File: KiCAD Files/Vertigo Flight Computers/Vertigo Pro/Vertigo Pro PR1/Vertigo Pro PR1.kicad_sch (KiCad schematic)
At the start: 140 parts, among them IC1 ICM-20602, IC2 DPS310XTSA1, IC3 MLX90393SLW-ABA-011-RE, J1 ST-LINK Conn, J2 USB_C_Receptacle_USB2.0, J3 FFC2A32-24-T, J4 Screw_Terminal, J5 Screw_Terminal, J6 Screw_Terminal, J7 Screw_Terminal, Q1 IRF530SPBF, Q2 IRF530SPBF, Q3 IRF530SPBF, Q4 IRF530SPBF, SW1 SW_SPDT, U1 STM32F103C8Tx, U10 TPS79133DBVR, U11 TLV709, U12 TLV709, U2 AP63203WU, U3 ESP32-S3-WROOM-1, U4 ME6211C28M5G-N, U5 ME6211C15M5G-N, U6 W25Q64FV, U7 TPS2121RUXR, U8 NEO-6M-GPS, U9 24AA32A-I_MS, Y1 16MHz

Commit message: sth
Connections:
- net STM_UART_RX is gone; now on net ESP_UART_TX: U1.31 (PA10), U8.20 (TXD1)
- net STM_UART_TX is gone; now on net ESP_UART_RX: U1.30 (PA9), U8.21 (RXD1)
- net ESP_UART_RX: now reaches U3.36 (RXD0)
- net ESP_UART_TX: now reaches U3.37 (TXD0)
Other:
- note added: "UART Communication MuCU/TuCU"
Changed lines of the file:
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@@
 	(wire
 		(pts
+			(xy 128.27 170.18) (xy 142.24 170.18)
+		)
+		(stroke
+			(width 0)
+			(type default)
+		)
+	)
+	(wire
+		(pts
 			(xy 58.42 262.89) (xy 69.85 262.89)
 		)
@@
 	(wire
 		(pts
+			(xy 158.75 144.78) (xy 187.96 144.78)
+		)
+		(stroke
+			(width 0)
+			(type default)
+		)
+	)
+	(wire
+		(pts
 			(xy 511.81 194.31) (xy 518.16 194.31)
 		)
@@
 	(wire
 		(pts
-			(xy 128.27 172.72) (xy 140.97 172.72)
+			(xy 128.27 172.72) (xy 142.24 172.72)
 		)
 		(stroke
@@
 	(wire
 		(pts
+			(xy 158.75 148.59) (xy 187.96 148.59)
+		)
+		(stroke
+			(width 0)
+			(type default)
+		)
+	)
+	(wire
+		(pts
 			(xy 486.41 288.29) (xy 501.65 288.29)
 		)
@@
 	(wire
 		(pts
-			(xy 128.27 175.26) (xy 140.97 175.26)
+			(xy 128.27 175.26) (xy 142.24 175.26)
 		)
 		(stroke
@@
 	(wire
 		(pts
+			(xy 128.27 167.64) (xy 142.24 167.64)
+		)
+		(stroke
+			(width 0)
+			(type default)
+		)
+	)
+	(wire
+		(pts
 			(xy 557.53 87.63) (xy 565.15 87.63)
 		)
@@
 		)
 	)
+	(text "UART Communication MuCU/TuCU"
+		(exclude_from_sim no)
+		(at 173.99 139.7 0)
+		(effects
+			(font
+				(size 1.27 1.27)
+			)
+		)
+	)
 	(text "Channel 4\n"
 		(exclude_from_sim no)
@@
 		)
 	)
+	(label "STM_UART_RX"
+		(at 187.96 148.59 180)
+		(fields_autoplaced yes)
+		(effects
+			(font
+				(size 1.27 1.27)
+			)
+			(justify right bottom)
+		)
+	)
 	(label "ESP_I2C_SCL"
 		(at 85.09 185.42 0)
@@
 		)
 	)
+	(label "ESP_UART_TX"
+		(at 158.75 148.59 0)
+		(fields_autoplaced yes)
+		(effects
+			(font
+				(size 1.27 1.27)
+			)
+			(justify left bottom)
+		)
+	)
 	(label "CAM_RESET"
 		(at 262.89 187.96 180)
@@
 		)
 	)
+	(label "STM_UART_TX"
+		(at 187.96 144.78 180)
+		(fields_autoplaced yes)
+		(effects
+			(font
+				(size 1.27 1.27)
+			)
+			(justify right bottom)
+		)
+	)
 	(label "BATT_U"
 		(at 167.64 80.01 180)
@@
 		)
 	)
+	(label "ESP_UART_RX"
+		(at 158.75 144.78 0)
+		(fields_autoplaced yes)
+		(effects
+			(font
+				(size 1.27 1.27)
+			)
+			(justify left bottom)
+		)
+	)
 	(label "CONTI_C1"
 		(at 31.75 50.8 0)
@@
 		)
 	)
+	(label "ESP_UART_TX"
+		(at 142.24 167.64 180)
+		(fields_autoplaced yes)
+		(effects
+			(font
+				(size 1.27 1.27)
+			)
+			(justify right bottom)
+		)
+	)
 	(label "DVP_Y7"
 		(at 262.89 200.66 180)
@@
 		)
 	)
+	(label "ESP_UART_RX"
+		(at 142.24 170.18 180)
+		(fields_autoplaced yes)
+		(effects
+			(font
+				(size 1.27 1.27)
+			)
+			(justify right bottom)
+		)
+	)
 	(label "VDD_1V5"
 		(at 307.34 219.71 0)
@@
 	)
 	(label "IO17"
-		(at 140.97 172.72 180)
+		(at 142.24 172.72 180)
 		(fields_autoplaced yes)
 		(effects
@@
 	)
 	(label "IO18"
-		(at 140.97 175.26 180)
+		(at 142.24 175.26 180)
 		(fields_autoplaced yes)
 		(effects

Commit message: footprinty
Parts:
- IC1: footprint (none) -> Vertigo Pro KiCad Libraries:PQFN50P300X300X80-16N
- IC2: footprint zswin:DPS310XTSA1 -> Vertigo Pro KiCad Libraries:DPS310XTSA1
- U11, U12: footprint (none) -> Vertigo Pro KiCad Libraries:SOT95P280X145-5N
- U6: footprint Vertigo Pro KiCad Libraries:SON127P600X800X80-9N -> Vertigo Pro KiCad Libraries:SON127P600X500X80-9N
- Y1: footprint (none) -> Vertigo Pro KiCad Libraries:XTAL_TSX-3225_16.0000MF09Z-AC6
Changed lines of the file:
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@@
 			)
 		)
-		(property "Footprint" ""
+		(property "Footprint" "Vertigo Pro KiCad Libraries:SOT95P280X145-5N"
 			(at 495.3 74.93 0)
 			(effects
@@
 			)
 		)
-		(property "Footprint" ""
+		(property "Footprint" "Vertigo Pro KiCad Libraries:XTAL_TSX-3225_16.0000MF09Z-AC6"
 			(at 171.45 257.81 0)
 			(effects
@@
 			)
 		)
-		(property "Footprint" "Vertigo Pro KiCad Libraries:SON127P600X800X80-9N"
+		(property "Footprint" "Vertigo Pro KiCad Libraries:SON127P600X500X80-9N"
 			(at 431.8 107.95 0)
 			(effects
@@
 			)
 		)
-		(property "Footprint" ""
+		(property "Footprint" "Vertigo Pro KiCad Libraries:PQFN50P300X300X80-16N"
 			(at 379.73 389.56 0)
 			(effects
@@
 			)
 		)
-		(property "Footprint" "zswin:DPS310XTSA1"
+		(property "Footprint" "Vertigo Pro KiCad Libraries:DPS310XTSA1"
 			(at 441.96 393.37 0)
 			(effects
@@
 			)
 		)
-		(property "Footprint" ""
+		(property "Footprint" "Vertigo Pro KiCad Libraries:SOT95P280X145-5N"
 			(at 528.32 30.48 0)
 			(effects

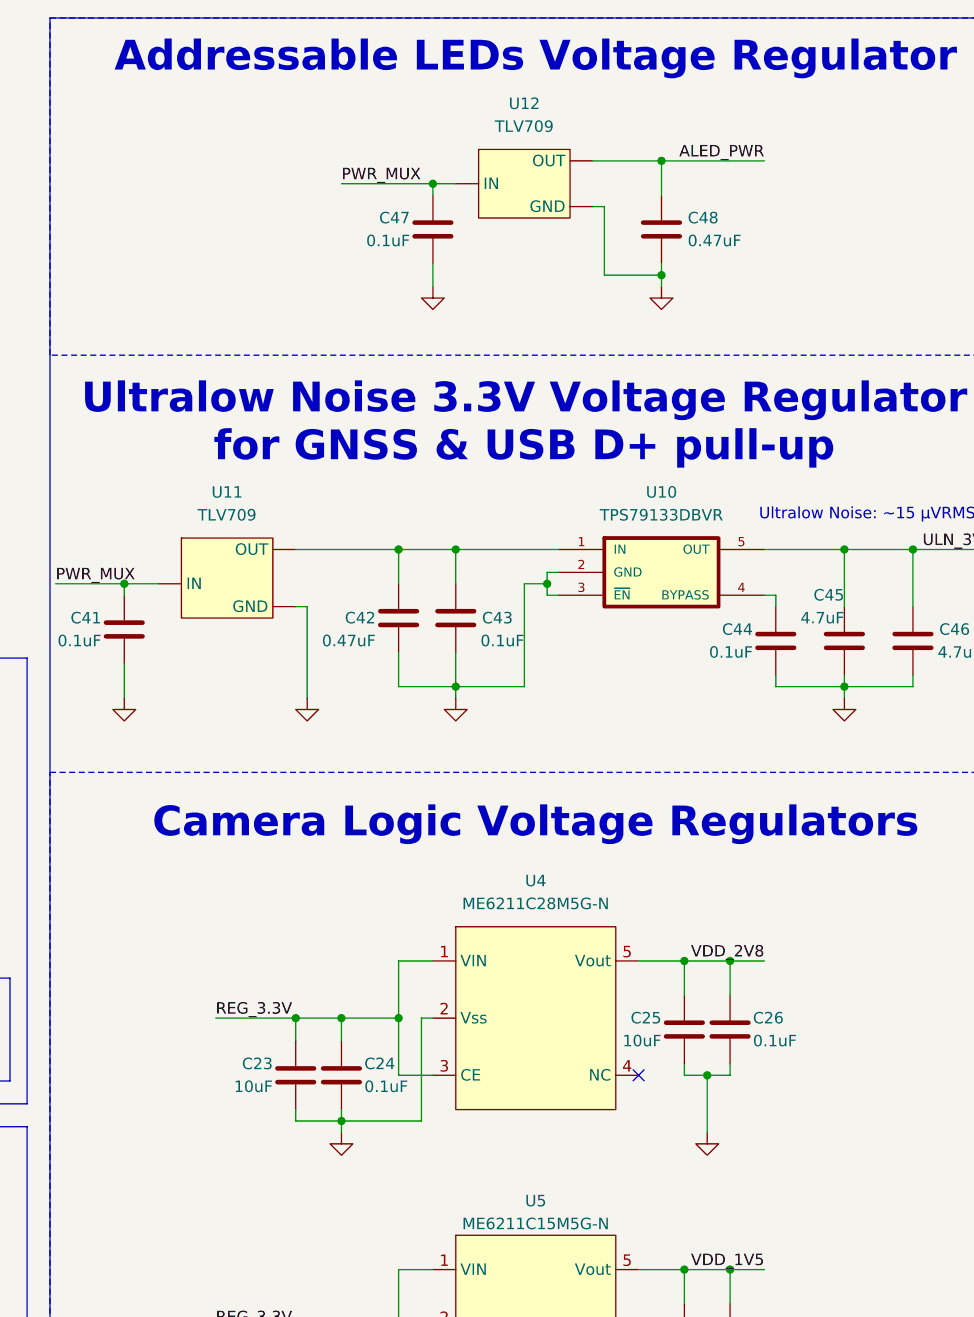
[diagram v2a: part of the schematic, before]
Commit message: New 2.8V cam voltage reg
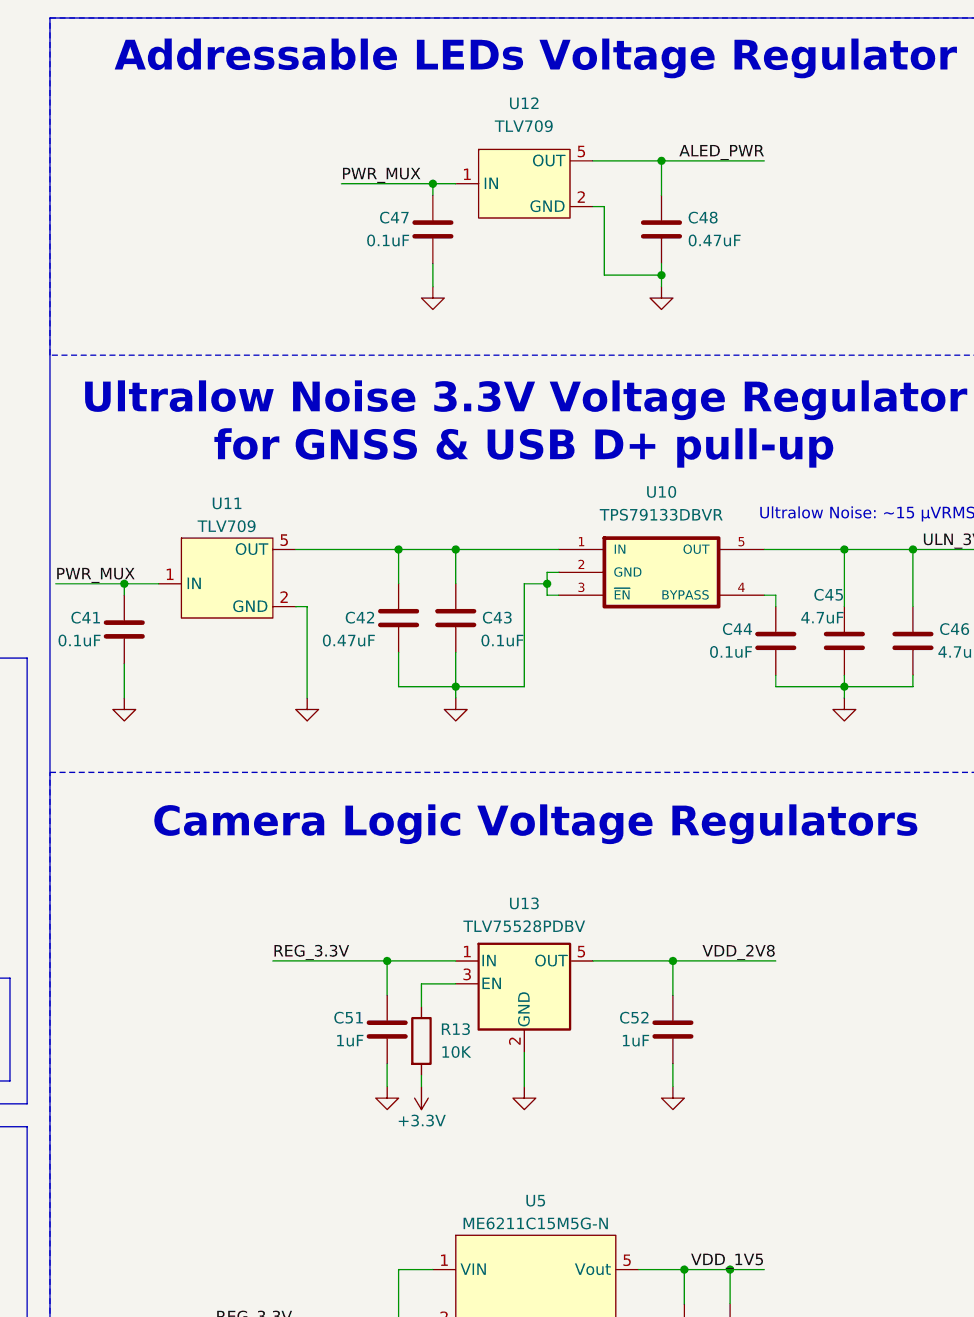
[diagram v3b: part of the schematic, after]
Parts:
- removed C23, C25: 10uF, Resistor_SMD:R_0603_1608Metric, symbol Device:C
- removed C24, C26: 0.1uF, Resistor_SMD:R_0402_1005Metric_Pad0.72x0.64mm_HandSolder, symbol Device:C
- removed U4: ME6211C28M5G-N, symbol Vertigo KiCad libraries:ME6211C28M5G-N
- added C51, C52: 1uF, Resistor_SMD:R_0603_1608Metric, symbol Device:C
- added R13: 10K, Resistor_SMD:R_0603_1608Metric, symbol Device:R
- added U13: TLV75528PDBV, Package_TO_SOT_SMD:SOT-23-5, symbol Regulator_Linear:TLV75528PDBV
- U10: footprint (none) -> Vertigo Pro KiCad Libraries:SOT95P280X145-5N
- U9: footprint (none) -> Vertigo Pro KiCad Libraries:SOP65P490X110-8N
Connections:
- net +3.3V: now also C51.2, R13.2, U13.1 (IN)
- net AGND: now also U11.2 (GND), U12.2 (GND), C51.1, C52.1, U13.2 (GND); no longer U11. (OUT), U12. (OUT)
- net ALED_PWR: now also U12.5 (OUT); no longer U12. (OUT)
- net DOVDD_2V8: now also C52.2, U13.5 (OUT)
- net PWR_MUX: now also U11.1 (IN), U12.1 (IN); no longer U11. (OUT), U12. (OUT)
- net at C42.2, C43.2, U10.1 (IN): now also U11.5 (OUT); no longer U11. (OUT)
- new net: R13.1, U13.3 (EN)
- no-connect marks 34 -> 33

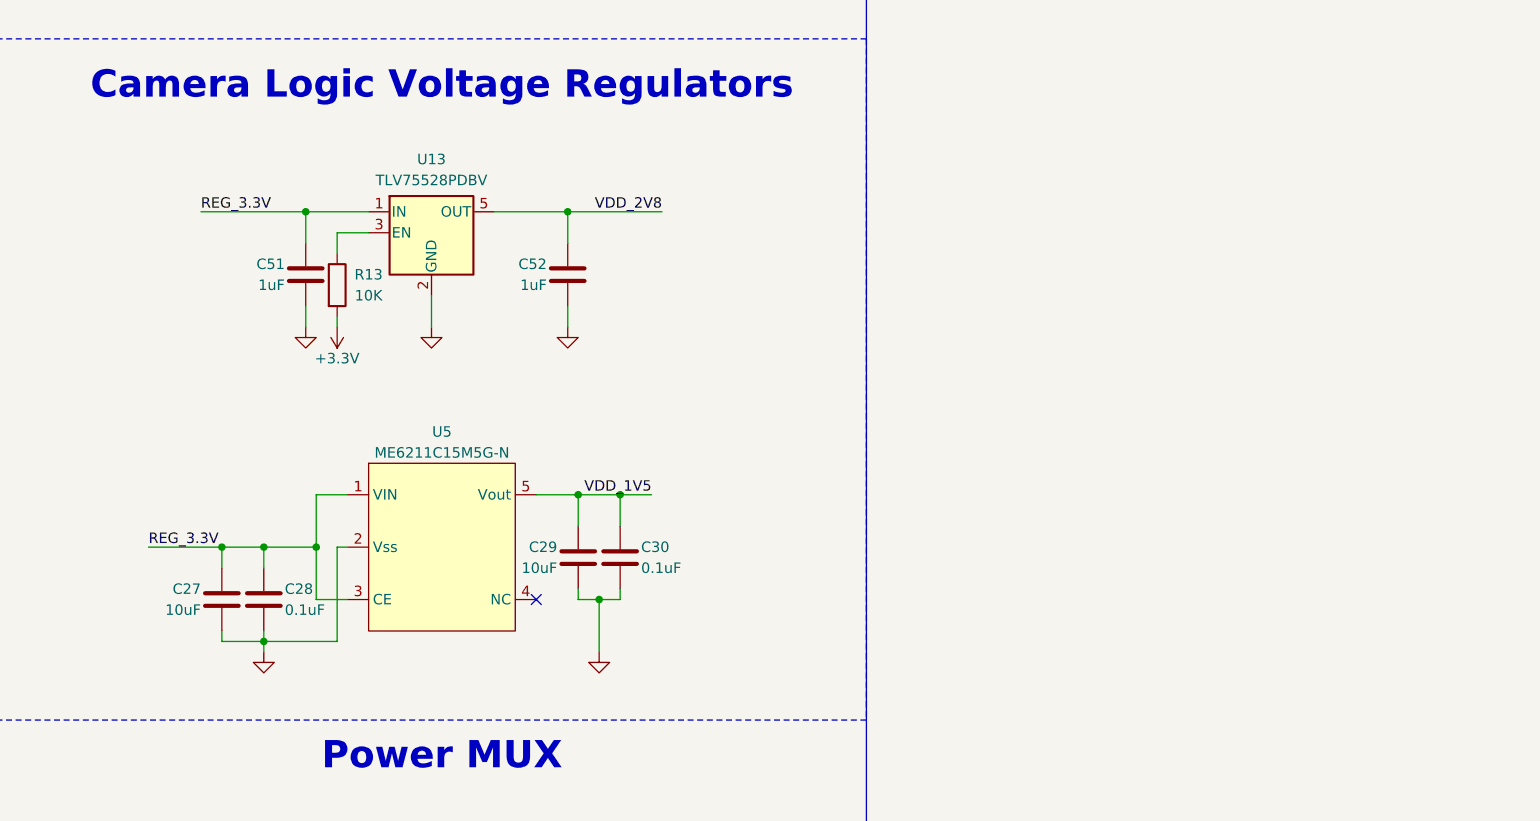
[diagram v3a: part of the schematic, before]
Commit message: 1.5V new cam voltage ldo
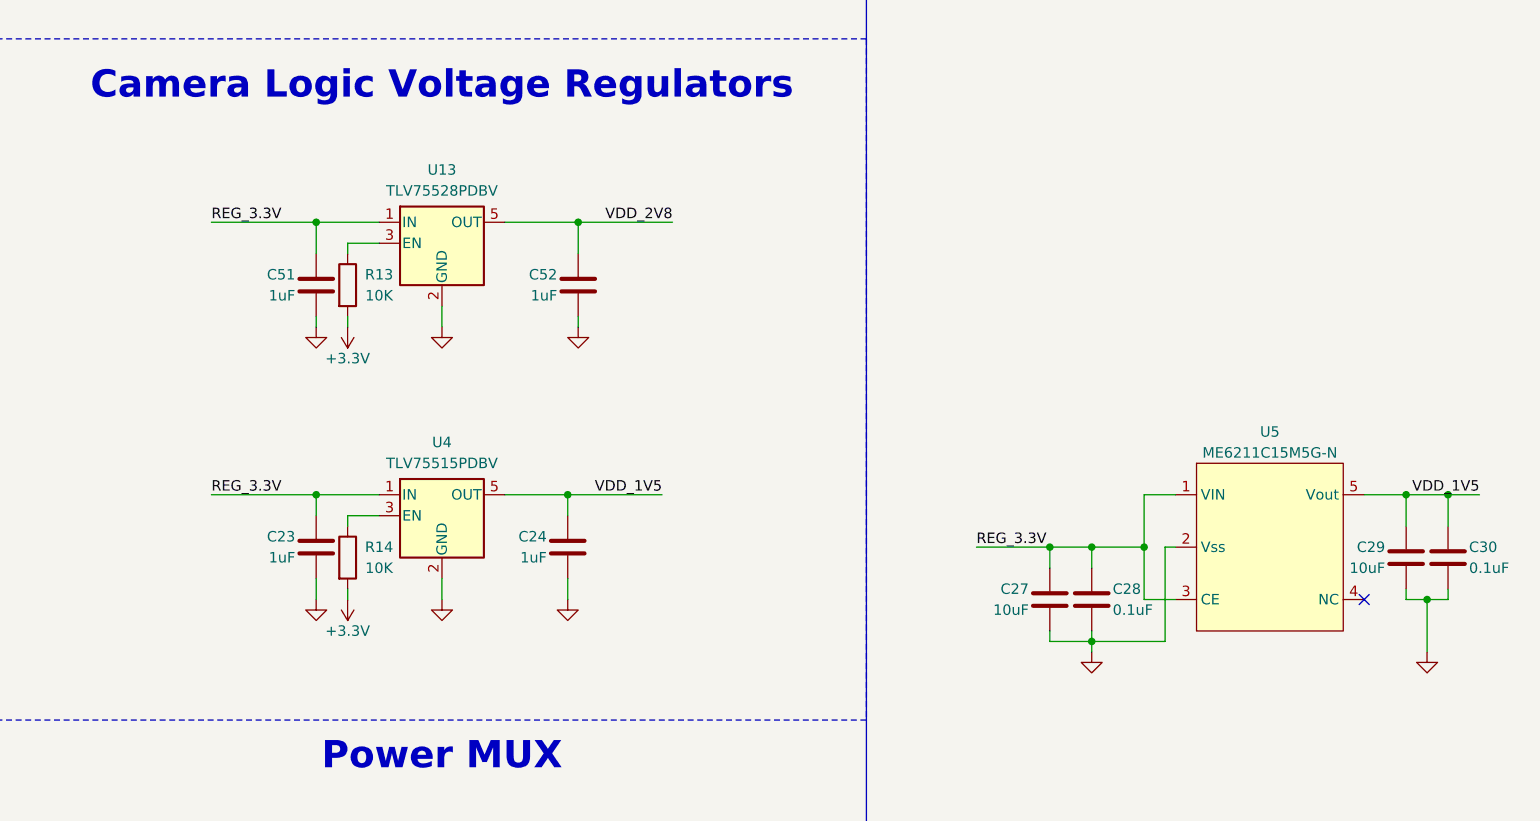
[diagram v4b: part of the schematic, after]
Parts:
- added C23, C24: 1uF, Resistor_SMD:R_0603_1608Metric, symbol Device:C
- added R14: 10K, Resistor_SMD:R_0603_1608Metric, symbol Device:R
- added U4: TLV75515PDBV, Package_TO_SOT_SMD:SOT-23-5, symbol Regulator_Linear:TLV75515PDBV
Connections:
- net +3.3V: now also C23.2, R14.2, U4.1 (IN)
- net AGND: now also C23.1, C24.1, U4.2 (GND)
- net DVDD_1V5: now also C24.2, U4.5 (OUT)
- new net: R14.1, U4.3 (EN)
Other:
- moved on the sheet: C27, C28, C29, C30, C51, C52, R13, U13, U5

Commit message: fix
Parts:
- removed C27, C29: 10uF, Resistor_SMD:R_0603_1608Metric, symbol Device:C
- removed C28, C30: 0.1uF, Resistor_SMD:R_0402_1005Metric_Pad0.72x0.64mm_HandSolder, symbol Device:C
- removed U5: ME6211C15M5G-N, symbol Vertigo KiCad libraries:ME6211C28M5G-N
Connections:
- no-connect marks 33 -> 32

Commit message: ESP Circuit fix
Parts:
- added C25: 1uF, Resistor_SMD:R_0603_1608Metric, symbol Device:C
- added C26: 0.1uF, Resistor_SMD:R_0402_1005Metric_Pad0.72x0.64mm_HandSolder, symbol Device:C
- added JP1, JP2: Jumper_2_Open, symbol Jumper:Jumper_2_Open
- C17: value 10uF -> 22uF
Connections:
- net AGND: now also C25.1, C26.1, JP1.1 (A), JP2.1 (A)
- net IO0: now reaches U3.27 (IO0)
- net IO0: now also JP2.2 (B)
- net ESP_EN: now reaches R12.2, U3.3 (EN)
- net ESP_EN: now also C25.2, C26.2, JP1.2 (B)
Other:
- note added: "Boot mode"
- note added: "Reset jumper"
- moved on the sheet: C16, C17, C51, D1, R12, R7, R8
